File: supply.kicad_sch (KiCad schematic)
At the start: 10 parts

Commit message: updated layout, power supply schematic
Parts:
- C7: footprint Capacitor_SMD:C_Elec_8x10.2 -> Capacitor_THT:C_Radial_D6.3mm_H11.0mm_P2.50mm
- C9: footprint Capacitor_SMD:C_Elec_8x10.2 -> Capacitor_THT:C_Radial_D8.0mm_H11.5mm_P3.50mm
- L1: value 47uH -> 100uH; footprint Inductor_SMD:L_7.3x7.3_H4.5 -> Vesc_footprints:100uH inductor 5x5mm
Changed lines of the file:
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@@
 			)
 		)
-		(property "Footprint" "Capacitor_SMD:C_Elec_8x10.2"
+		(property "Footprint" "Capacitor_THT:C_Radial_D8.0mm_H11.5mm_P3.50mm"
 			(at 141.9352 68.58 0)
 			(hide yes)
@@
 			)
 		)
-		(property "Value" "47uH"
+		(property "Value" "100uH"
 			(at 125.73 57.15 90)
 			(show_name no)
@@
 			)
 		)
-		(property "Footprint" "Inductor_SMD:L_7.3x7.3_H4.5"
+		(property "Footprint" "Vesc_footprints:100uH inductor 5x5mm"
 			(at 125.73 59.69 0)
 			(hide yes)
@@
 			)
 		)
-		(property "Footprint" "Capacitor_SMD:C_Elec_8x10.2"
+		(property "Footprint" "Capacitor_THT:C_Radial_D6.3mm_H11.0mm_P2.50mm"
 			(at 73.3552 55.88 0)
 			(hide yes)

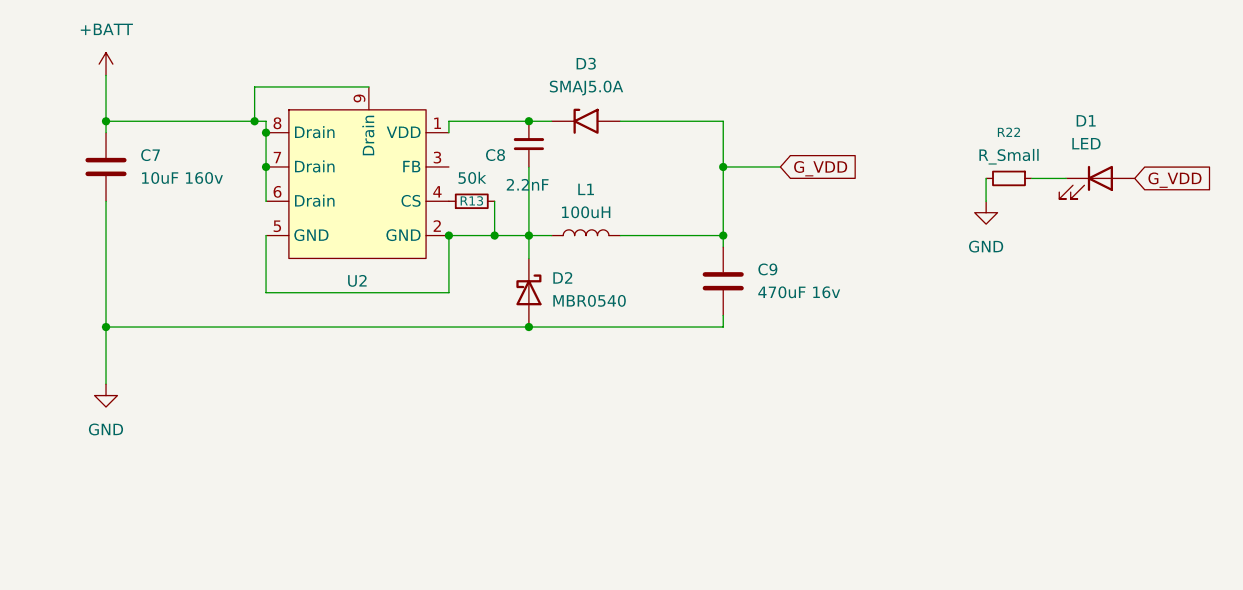
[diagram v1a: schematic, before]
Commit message: Fix ESC power, gate drive and current sensing schematics
Correct the buck converter and MCU symbols, bootstrap networks, MOSFET pulldowns and current sensing components. Migrate project libraries, synchronize PCB footprints and ground nets, and resolve ERC errors and warnings. Include LCSC BOMs and design notes; PCB routing remains incomplete.
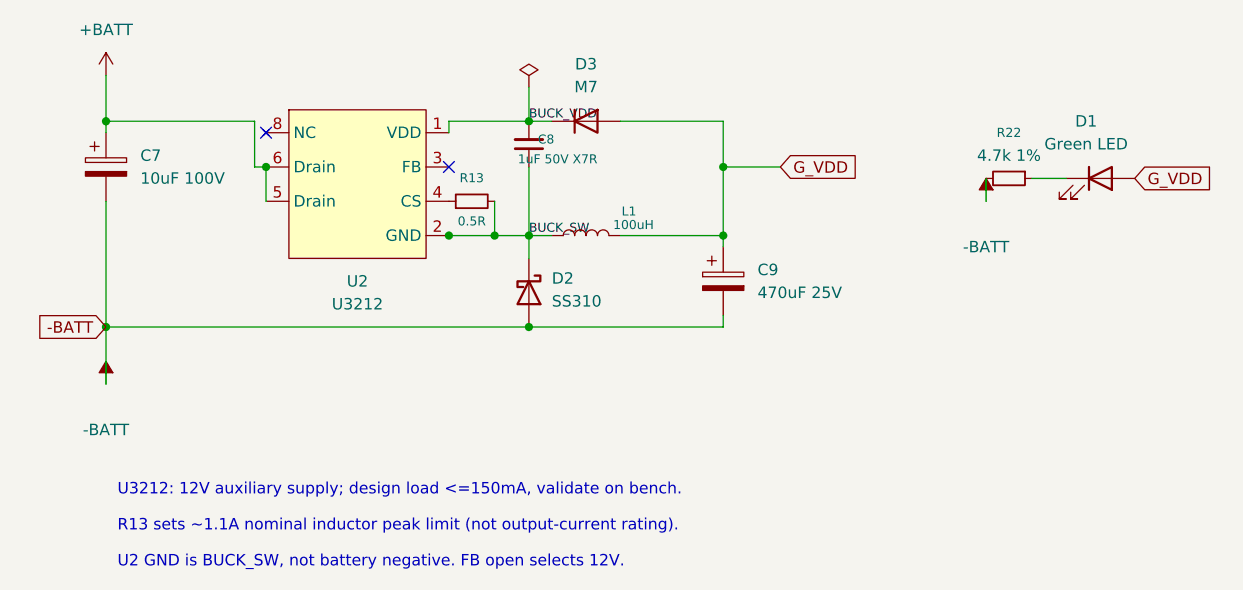
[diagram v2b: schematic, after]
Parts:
- C7: value 10uF 160v -> 10uF 100V; symbol Device:C -> Device:C_Polarized; LCSC (none) -> C106677; MPN (none) -> ERS1KM100E11OT; Manufacturer (none) -> AISHI
- C8: value 2.2nF -> 1uF 50V X7R; LCSC (none) -> C376929; MPN (none) -> TCC0805X7R105M500FT; Manufacturer (none) -> CCTC
- C9: value 470uF 16v -> 470uF 25V; footprint Capacitor_THT:C_Radial_D8.0mm_H11.5mm_P3.50mm -> Custom_footprints:C_Radial_D8.0mm_H12.0mm_P3.50mm; symbol Device:C -> Device:C_Polarized; LCSC (none) -> C503221; MPN (none) -> 01EC1227SHC470UF25V; Manufacturer (none) -> KNSCHA
- D1: value LED -> Green LED; LCSC (none) -> C72043; MPN (none) -> 19-217/GHC-YR1S2/3T; Manufacturer (none) -> EVERLIGHT
- D2: value MBR0540 -> SS310; footprint Diode_SMD:D_SOD-123 -> Diode_SMD:D_SMA; LCSC (none) -> C513470; MPN (none) -> SS310; Manufacturer (none) -> Slkor
- D3: value SMAJ5.0A -> M7; symbol Diode:SMAJ5.0A -> Device:D; LCSC (none) -> C266550; MPN (none) -> M7; Manufacturer (none) -> BORN
- L1: footprint Vesc_footprints:100uH inductor 5x5mm -> Custom_footprints:L_XR_XR0650; LCSC (none) -> C5358146; MPN (none) -> XR0650-101M; Manufacturer (none) -> XR
- R13: value 50k -> 0.5R; footprint Resistor_SMD:R_0402_1005Metric_Pad0.72x0.64mm_HandSolder -> Resistor_SMD:R_1206_3216Metric_Pad1.30x1.75mm_HandSolder; LCSC (none) -> C2759131; MPN (none) -> HP06W2F500LT5E; Manufacturer (none) -> UNI-ROYAL
- R22: value R_Small -> 4.7k 1%; LCSC (none) -> C23162; MPN (none) -> 0603WAF4701T5E; Manufacturer (none) -> UNI-ROYAL
- U2: value (none) -> U3212; footprint Package_SO:SOIC-8-1EP_3.9x4.9mm_P1.27mm_EP2.62x3.51mm -> Custom_footprints:U3212_SOP-7_3.9x4.9mm_P1.27mm; symbol LINKOSEMI_LKS32MC034SF6M8:u2312_buck_controller -> Custom:U3212; LCSC (none) -> C2874740; MPN (none) -> U3212; Manufacturer (none) -> UNI-SEMIC
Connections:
- net +BATT: now also U2.5 (Drain); no longer U2.7 (Drain), U2.8 (Drain), U2.9 (Drain)
- net BUCK_VDD: now reaches C8.2, D3.1 (K), U2.1 (VDD)
- net BUCK_SW: now reaches C8.1, D2.1 (K), L1.1, R13.2, U2.2 (GND)
- net BUCK_SW: no longer U2.5 (GND)
- net GND renamed -BATT
- no-connect marks 0 -> 2
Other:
- note added: "R13 sets ~1.1A nominal inductor peak limit (not output-current rating)."
- note added: "U2 GND is BUCK_SW, not battery negative. FB open selects 12V."
- note added: "U3212: 12V auxiliary supply; design load <=150mA, validate on bench."
